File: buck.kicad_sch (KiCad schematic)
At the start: 5 parts, among them U3 LM2596S-ADJ

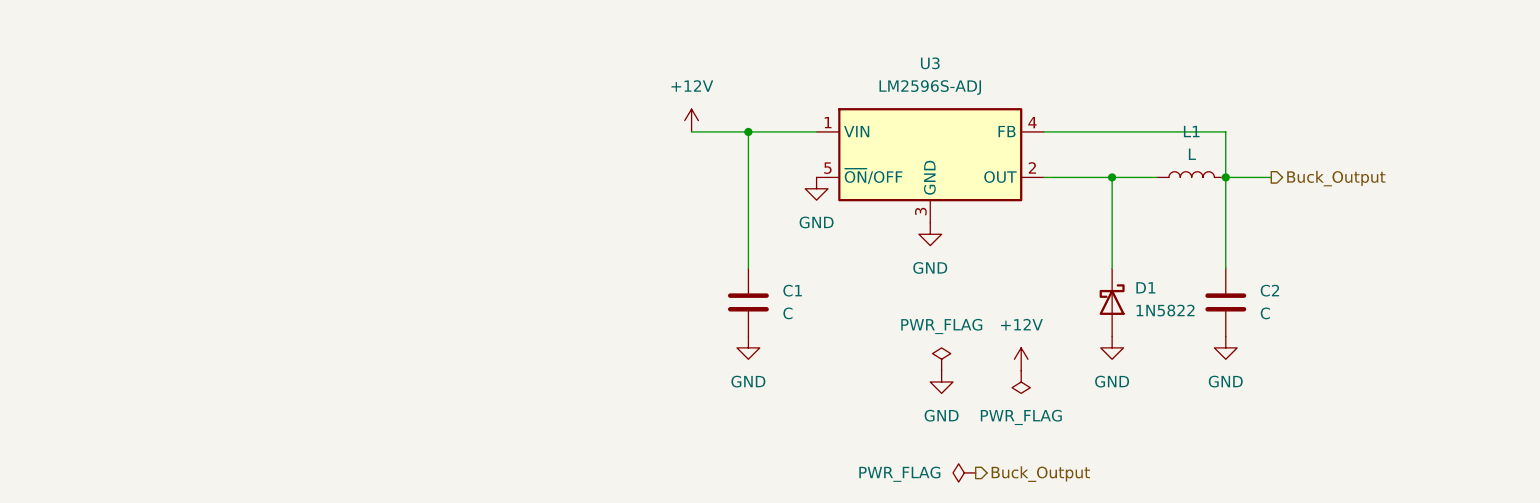
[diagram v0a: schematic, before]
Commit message: Finished AudioAmplifier + Added Values
Added Buck Coverter components values, finished audio amplifier
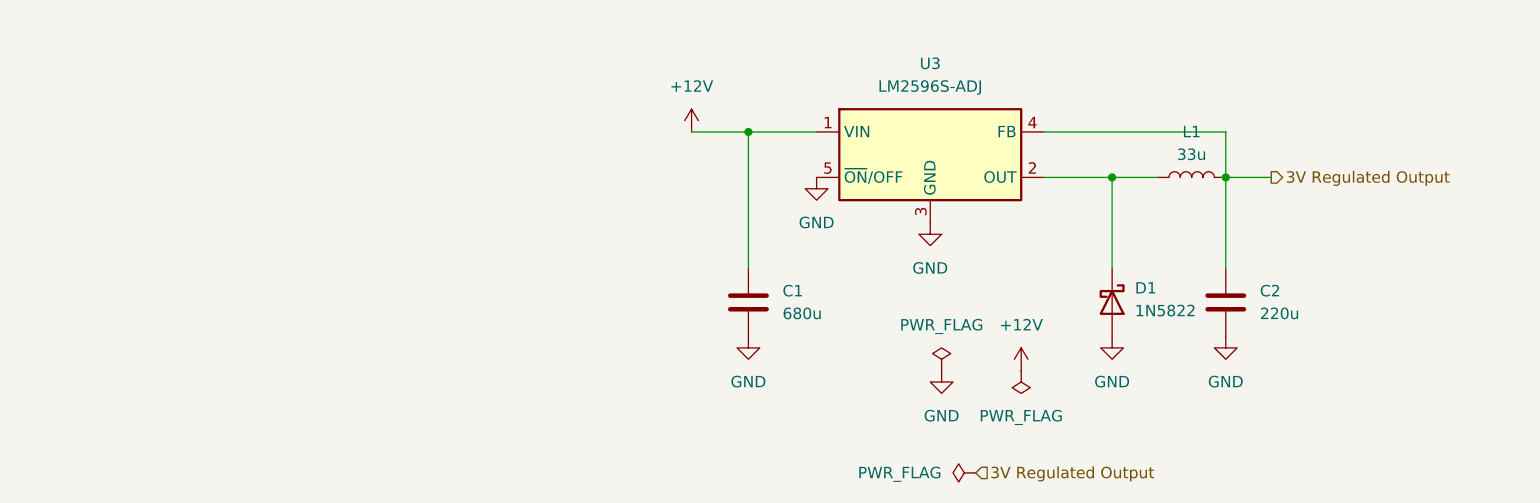
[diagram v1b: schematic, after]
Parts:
- C1: value C -> 680u
- C2: value C -> 220u
- L1: value L -> 33u
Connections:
- net Buck_Output renamed 3V Regulated Output
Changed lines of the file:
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@@
 		)
 	)
-	(hierarchical_label "Buck_Output"
+	(hierarchical_label "3V Regulated Output"
 		(shape output)
 		(at 165.1 77.47 0)
@@
 		)
 	)
-	(hierarchical_label "Buck_Output"
-		(shape output)
+	(hierarchical_label "3V Regulated Output"
+		(shape input)
 		(at 132.08 110.49 0)
 		(fields_autoplaced yes)
@@
 			)
 		)
-		(property "Value" "L"
+		(property "Value" "33u"
 			(at 156.21 74.93 90)
 			(effects
@@
 			)
 		)
-		(property "Value" "C"
+		(property "Value" "680u"
 			(at 110.49 92.7099 0)
 			(effects
@@
 			)
 		)
-		(property "Value" "C"
+		(property "Value" "220u"
 			(at 163.83 92.7099 0)
 			(effects

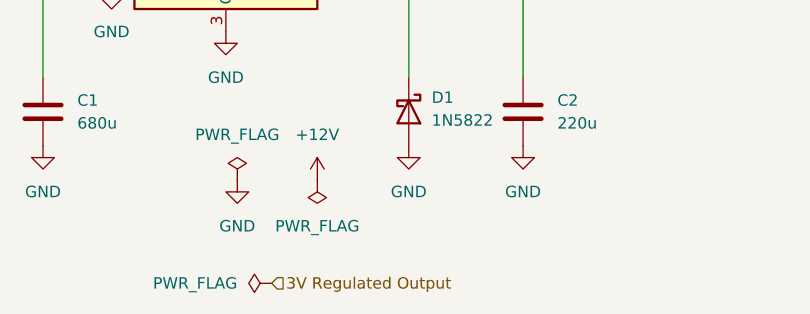
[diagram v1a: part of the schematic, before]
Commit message: Set 3.3 Output from Buck
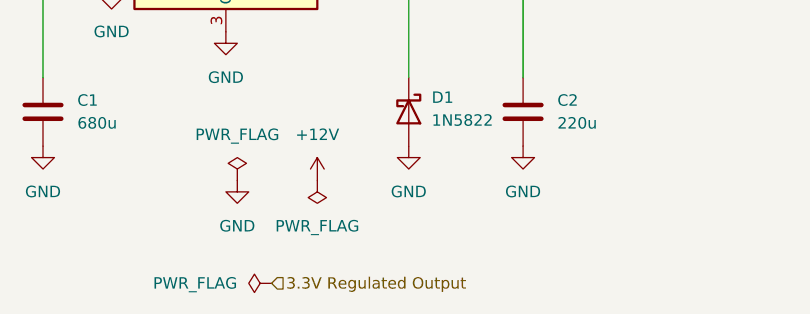
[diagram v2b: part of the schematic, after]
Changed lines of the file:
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@@
 		)
 	)
-	(hierarchical_label "3V Regulated Output"
+	(hierarchical_label "3.3V Regulated Output"
 		(shape input)
 		(at 132.08 110.49 0)

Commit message: Cleanup, sorting, adding external parts
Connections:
- net 3V Regulated Output is gone; now on net 3.3V Regulated Output: C2.1, L1.1, U3.4 (FB)
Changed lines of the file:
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@@
 		)
 	)
-	(hierarchical_label "3V Regulated Output"
+	(hierarchical_label "3.3V Regulated Output"
 		(shape output)
 		(at 165.1 77.47 0)

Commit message: Added a jack for power supply
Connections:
- net +12V renamed 12V_IN

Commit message: Switched model of buck converter
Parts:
- removed U3: LM2596S-ADJ, Package_TO_SOT_SMD:TO-263-5_TabPin3, symbol Regulator_Switching:LM2596S-ADJ
- added U4: LM2596S-5, Package_TO_SOT_SMD:TO-263-5_TabPin3, symbol Regulator_Switching:LM2596S-5
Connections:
- net 12V_IN: now also U4.1 (VIN)
- net GND: now also U4.3 (GND), U4.5 (~{ON}/OFF)
- net at D1.1 (K), L1.2: now also U4.2 (OUT)
- net 3.3V Regulated Output renamed 5V_OUT
- net 5V_OUT: now also U4.4 (FB)
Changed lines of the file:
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@@
 		)
 	)
-	(hierarchical_label "3.3V Regulated Output"
+	(hierarchical_label "5V_OUT"
 		(shape output)
 		(at 165.1 77.47 0)
@@
 		)
 	)
-	(hierarchical_label "3.3V Regulated Output"
+	(hierarchical_label "5V_OUT"
 		(shape input)
 		(at 132.08 110.49 0)
@@
 	)
 	(symbol
+		(lib_id "Regulator_Switching:LM2596S-5")
+		(at 127 74.93 0)
+		(unit 1)
+		(exclude_from_sim no)
+		(in_bom yes)
+		(on_board yes)
+		(dnp no)
+		(fields_autoplaced yes)
+		(property "Reference" "U4"
+			(at 127 64.77 0)
+			(effects
+				(font
+					(size 1.27 1.27)
+				)
+			)
+		)
+		(property "Value" "LM2596S-5"
+			(at 127 67.31 0)
+			(effects
+				(font
+					(size 1.27 1.27)
+				)
+			)
+		)
+		(property "Footprint" "Package_TO_SOT_SMD:TO-263-5_TabPin3"
+			(at 128.27 81.28 0)
+			(effects
+				(font
+					(size 1.27 1.27)
+					(italic yes)
+				)
+				(justify left)
+				(hide yes)
+			)
+		)
+		(property "Datasheet" "http://www.ti.com/lit/ds/symlink/lm2596.pdf"
+			(at 127 74.93 0)
+			(effects
+				(font
+					(size 1.27 1.27)
+				)
+				(hide yes)
+			)
+		)
+		(property "Description" "5V 3A Step-Down Voltage Regulator, TO-263"
+			(at 127 74.93 0)
+			(effects
+				(font
+					(size 1.27 1.27)
+				)
+				(hide yes)
+			)
+		)
+		(pin "1"
+		)
+		(pin "2"
+		)
+		(pin "4"
+		)
+		(pin "3"
+		)
+		(pin "5"
+		)
+		(instances
+			(project ""
+				(path "/23b35dcc-615e-4aec-abee-c26cc3d8b906/57a337a3-c367-4ad3-adc0-1aeb321dd5f9"
+					(reference "U4")
+					(unit 1)
+				)
+			)
+		)
+	)
+	(symbol
 		(lib_id "power:GND")
 		(at 114.3 77.47 0)
@@
 					(unit 1)
 				)
-			)
-		)
-	)
-	(symbol
-		(lib_id "Regulator_Switching:LM2596S-ADJ")
-		(at 127 74.93 0)
-		(unit 1)
-		(exclude_from_sim no)
-		(in_bom yes)
-		(on_board yes)
-		(dnp no)
-		(fields_autoplaced yes)
-		(property "Reference" "U3"
-			(at 127 64.77 0)
-			(effects
-				(font
-					(size 1.27 1.27)
-				)
-			)
-		)
-		(property "Value" "LM2596S-ADJ"
-			(at 127 67.31 0)
-			(effects
-				(font
-					(size 1.27 1.27)
-				)
-			)
-		)
-		(property "Footprint" "Package_TO_SOT_SMD:TO-263-5_TabPin3"
-			(at 128.27 81.28 0)
-			(effects
-				(font
-					(size 1.27 1.27)
-					(italic yes)
-				)
-				(justify left)
-				(hide yes)
-			)
-		)
-		(property "Datasheet" "http://www.ti.com/lit/ds/symlink/lm2596.pdf"
-			(at 127 74.93 0)
-			(effects
-				(font
-					(size 1.27 1.27)
-				)
-				(hide yes)
-			)
-		)
-		(property "Description" "Adjustable 3A Step-Down Voltage Regulator, TO-263"
-			(at 127 74.93 0)
-			(effects
-				(font
-					(size 1.27 1.27)
-				)
-				(hide yes)
-			)
-		)
-		(pin "2"
-		)
-		(pin "4"
-		)
-		(pin "5"
-		)
-		(pin "3"
-		)
-		(pin "1"
-		)
-		(instances
-			(project "plant caretaker"
-				(path "/23b35dcc-615e-4aec-abee-c26cc3d8b906/57a337a3-c367-4ad3-adc0-1aeb321dd5f9"
-					(reference "U3")
-					(unit 1)
-				)

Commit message: Added basic footprint to ESP32
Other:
- title: (none) -> Buck converter
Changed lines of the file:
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@@
 	(generator_version "8.0")
 	(paper "A4")
+	(title_block
+		(title "Buck converter")
+		(date "2024-12-12")
+	)
 	(junction
 		(at 160.02 77.47)
@@
 		)
 		(instances
-			(project ""
+			(project "plant caretaker"
 				(path "/23b35dcc-615e-4aec-abee-c26cc3d8b906/57a337a3-c367-4ad3-adc0-1aeb321dd5f9"
 					(reference "U4")

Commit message: Added footprints and imported to PCB
All of them except speakers
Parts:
- C1: footprint (none) -> Capacitor_SMD:CP_Elec_10x12.5
- C2: footprint (none) -> Capacitor_SMD:CP_Elec_6.3x7.7
- D1: footprint Diode_THT:D_DO-201AD_P15.24mm_Horizontal -> Diode_SMD:D_0603_1608Metric
- L1: footprint (none) -> Inductor_SMD:L_0603_1608Metric
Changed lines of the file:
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@@
 			)
 		)
-		(property "Footprint" ""
+		(property "Footprint" "Inductor_SMD:L_0603_1608Metric"
 			(at 156.21 77.47 0)
 			(effects
@@
 			)
 		)
-		(property "Footprint" ""
+		(property "Footprint" "Capacitor_SMD:CP_Elec_10x12.5"
 			(at 107.6452 95.25 0)
 			(effects
@@
 			)
 		)
-		(property "Footprint" ""
+		(property "Footprint" "Capacitor_SMD:CP_Elec_6.3x7.7"
 			(at 160.9852 95.25 0)
 			(effects
@@
 			)
 		)
-		(property "Footprint" "Diode_THT:D_DO-201AD_P15.24mm_Horizontal"
+		(property "Footprint" "Diode_SMD:D_0603_1608Metric"
 			(at 142.875 91.44 0)
 			(effects

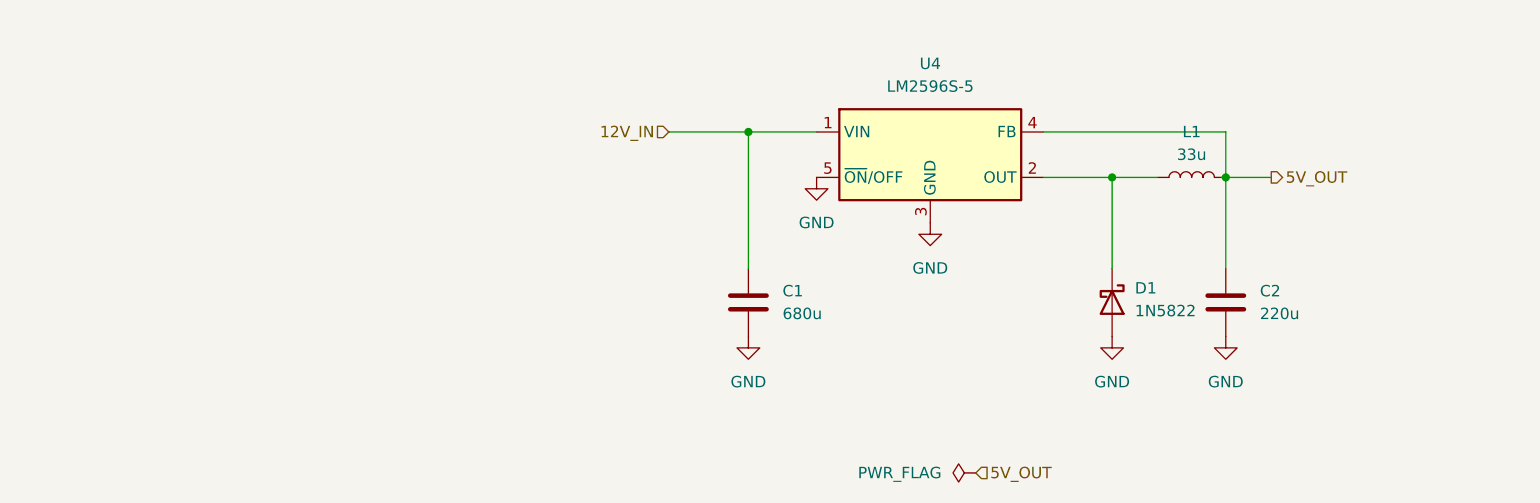
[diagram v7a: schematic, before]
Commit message: Moved Pump to Buck
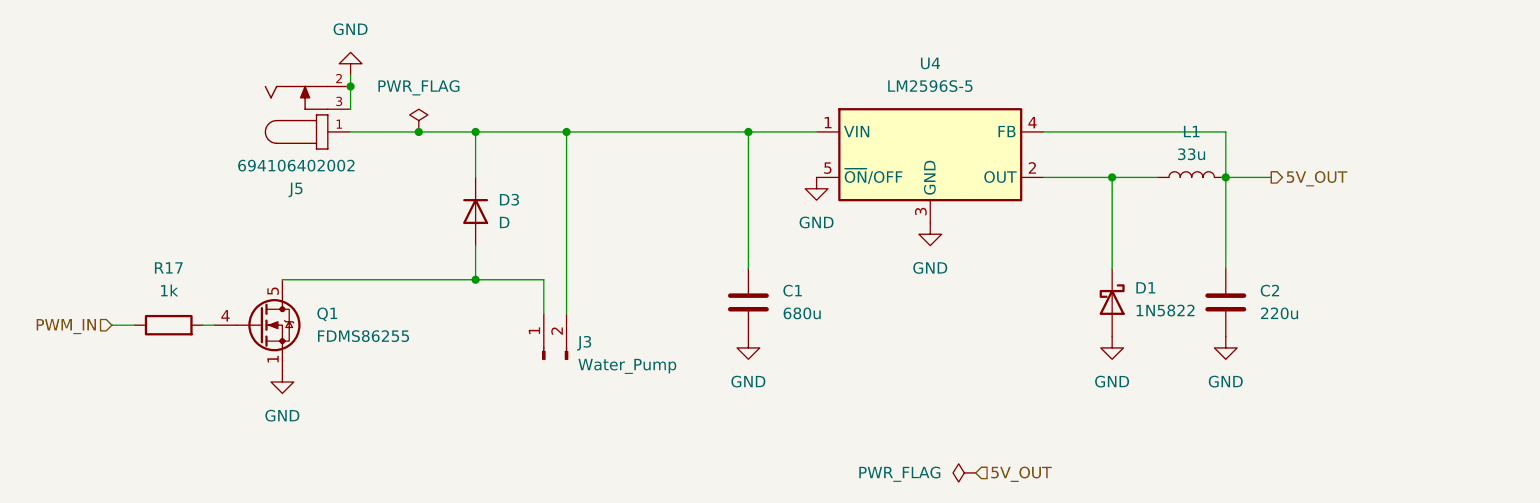
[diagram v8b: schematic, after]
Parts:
- added D3: D, Diode_SMD:D_0603_1608Metric, symbol Device:D
- added J3: Water_Pump, Connector_PinHeader_1.00mm:PinHeader_1x02_P1.00mm_Vertical_SMD_Pin1Right, symbol Connector:Conn_01x02_Pin
- added J5: 694106402002, Connector_BarrelJack:BarrelJack_Wuerth_694106106102_2.0x5.5mm, symbol 694106402002:694106402002
- added Q1: FDMS86255, Package_TO_SOT_SMD:TDSON-8-1, symbol Transistor_FET:FDMS86255
- added R17: 1k, Resistor_SMD:R_0603_1608Metric, symbol Device:R
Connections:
- net GND: now also J5.2, J5.3, Q1.1 (S), Q1.2 (S), Q1.3 (S)
- net 12V_IN: no longer names the net of C1.1, U4.1 (VIN)
- net 12V_IN: now also D3.1 (K), J3.2 (Pin_2), J5.1
- new net: D3.2 (A), J3.1 (Pin_1), Q1.5 (D)
- new net: Q1.4 (G), R17.2
- new net PWM_IN: R17.1
